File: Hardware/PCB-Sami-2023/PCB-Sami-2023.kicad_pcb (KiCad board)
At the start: 2 copper layers, 75 x 40.2 mm, 44 parts, among them J10 Bateria, J9 STEP_DOWN, P1 TatamiDerecho, P2 TatamiIzquierdo, P3 SharpDerecho, P4 SharpIzquierdo, P5 LDR, P6 MotorIzquierdo, P7 MotorDerecho, P8 Pantalla Oled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

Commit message: agregue ultimos detalles
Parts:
- removed the ? at (113.1, 61.6)
- removed the ? at (113.1, 76.6)
- removed the ? at (113.1, 82.9)
- removed the ? at (135.0, 87.8)
- removed the ? at (113.1, 55.3)
- removed the ? at (146.0, 87.8)
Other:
- board size 75 x 40.2 mm -> 75 x 40 mm
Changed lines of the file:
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@@
     (pad_to_mask_clearance 0)
     (pcbplotparams
-      (layerselection 0x0000010_7ffffffe)
+      (layerselection 0x0000020_7ffffffe)
       (plot_on_all_layers_selection 0x0001000_00000000)
       (disableapertmacros false)
@@
         (effects (font (size 1.27 1.27) (thickness 0.15)))
     )
-    (pad "1" thru_hole circle (at 0 0 180) (size 2 2) (drill 1.00076) (layers "*.Cu" "*.Mask" "F.SilkS")
-      (net 2 "+5V") (pinfunction "1") (pintype "passive"))
-  )
-  (footprint "" (layer "F.Cu")
-    (at 113.1 76.6)
-    (fp_text reference "" (at 0 0) (layer "F.SilkS")
-        (effects (font (size 1.27 1.27) (thickness 0.15)))
-    )
-    (fp_text value "" (at 0 0) (layer "F.SilkS")
-        (effects (font (size 1.27 1.27) (thickness 0.15)))
-    )
     (pad "2" thru_hole circle (at 0 0 180) (size 2 2) (drill 1.00076) (layers "*.Cu" "*.Mask" "F.SilkS")
       (net 6 "/START") (pinfunction "2") (pintype "passive"))
   )
-  (footprint "" (layer "F.Cu")
-    (at 135 87.8)
-    (fp_text reference "" (at 0 0) (layer "F.SilkS")
-        (effects (font (size 1.27 1.27) (thickness 0.15)))
-    )
-    (fp_text value "" (at 0 0) (layer "F.SilkS")
-        (effects (font (size 1.27 1.27) (thickness 0.15)))
-    )
-    (pad "1" thru_hole circle (at 0 0 180) (size 2 2) (drill 1.00076) (layers "*.Cu" "*.Mask" "F.SilkS")
-      (net 2 "+5V") (pinfunction "1") (pintype "passive"))
-  )
-  (footprint "" (layer "F.Cu")
-    (at 113.1 55.3)
-    (fp_text reference "" (at 0 0) (layer "F.SilkS")
-        (effects (font (size 1.27 1.27) (thickness 0.15)))
-    )
-    (fp_text value "" (at 0 0) (layer "F.SilkS")
-        (effects (font (size 1.27 1.27) (thickness 0.15)))
-    )
-    (pad "1" thru_hole circle (at 0 0 180) (size 2 2) (drill 1.00076) (layers "*.Cu" "*.Mask" "F.SilkS")
-      (net 2 "+5V") (pinfunction "1") (pintype "passive"))
-  )
-  (footprint "" (layer "F.Cu")
-    (at 146 87.8)
-    (fp_text reference "" (at 0 0) (layer "F.SilkS")
-        (effects (font (size 1.27 1.27) (thickness 0.15)))
-    )
-    (fp_text value "" (at 0 0) (layer "F.SilkS")
-        (effects (font (size 1.27 1.27) (thickness 0.15)))
-    )
-    (pad "1" thru_hole circle (at 0 0 180) (size 2 2) (drill 1.00076) (layers "*.Cu" "*.Mask" "F.SilkS")
-      (net 2 "+5V") (pinfunction "1") (pintype "passive"))
-  )
   (footprint "EESTN5:Pin_Header_2" (layer "F.Cu")
     (at 177.93 57.2525 180)
@@
       (stroke (width 0) (type solid)) (fill solid) (layer "B.Cu"))
   )
-  (footprint "" (layer "F.Cu")
-    (at 113.1 61.6)
-    (fp_text reference "" (at 0 0) (layer "F.SilkS")
-        (effects (font (size 1.27 1.27) (thickness 0.15)))
-    )
-    (fp_text value "" (at 0 0) (layer "F.SilkS")
-        (effects (font (size 1.27 1.27) (thickness 0.15)))
-    )
-    (pad "1" thru_hole circle (at 0 0 180) (size 2 2) (drill 1.00076) (layers "*.Cu" "*.Mask" "F.SilkS")
-      (net 2 "+5V") (pinfunction "1") (pintype "passive"))
-  )
   (footprint "EESTN5:Pin_Header_2" (layer "F.Cu")
     (at 177.93 61.6175 180)
@@
       (net 6 "/START") (pinfunction "2") (pintype "passive"))
   )
-  (footprint "" (layer "F.Cu")
-    (at 113.1 82.9)
-    (fp_text reference "" (at 0 0) (layer "F.SilkS")
-        (effects (font (size 1.27 1.27) (thickness 0.15)))
-    )
-    (fp_text value "" (at 0 0) (layer "F.SilkS")
-        (effects (font (size 1.27 1.27) (thickness 0.15)))
-    )
-    (pad "1" thru_hole circle (at 0 0 180) (size 2 2) (drill 1.00076) (layers "*.Cu" "*.Mask" "F.SilkS")
-      (net 2 "+5V") (pinfunction "1") (pintype "passive"))
-  )
   (footprint "footprints:JstXH4P" (layer "F.Cu")
     (at 158.3 87.275)
@@
         (effects (font (size 1 1) (thickness 0.15)))
     )
-    (fp_text value "SharpDerecho" (at 0 -1.9) (layer "F.SilkS")
+    (fp_text value "SharpDerecho" (at 10.5 -1.93) (layer "F.SilkS")
         (effects (font (size 1 1) (thickness 0.15)))
     )
@@
   (gr_line (start 106.9 51.65) (end 106.9 91.65)
     (stroke (width 0.1) (type default)) (layer "Edge.Cuts"))
-  (gr_line (start 181.9 91.65) (end 181.9 51.5)
+  (gr_line (start 181.9 91.65) (end 181.9 51.7)
     (stroke (width 0.1) (type default)) (layer "Edge.Cuts"))
   (gr_line (start 181.9 51.65) (end 106.9 51.65)

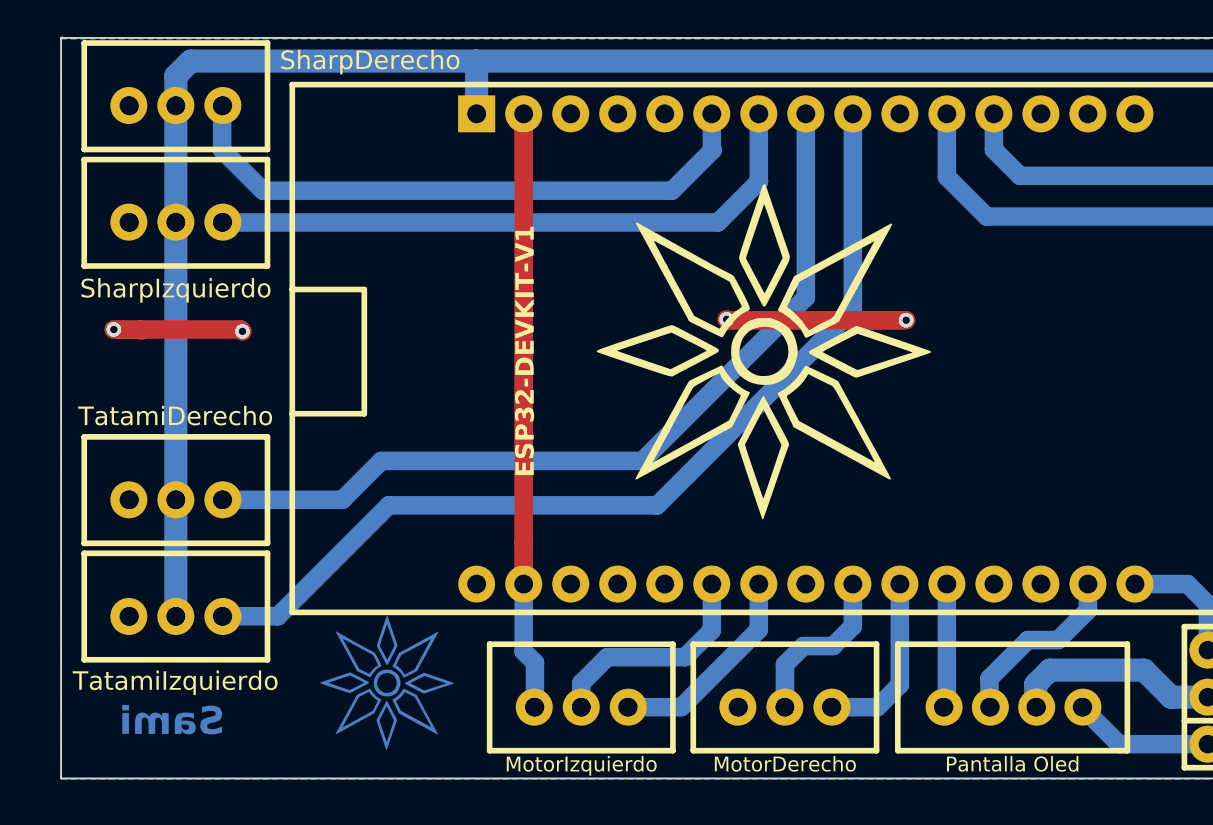
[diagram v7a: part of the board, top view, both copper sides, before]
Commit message: Cambio en el pinout de los motores y unas correcciones de codigos luego de probar el robots
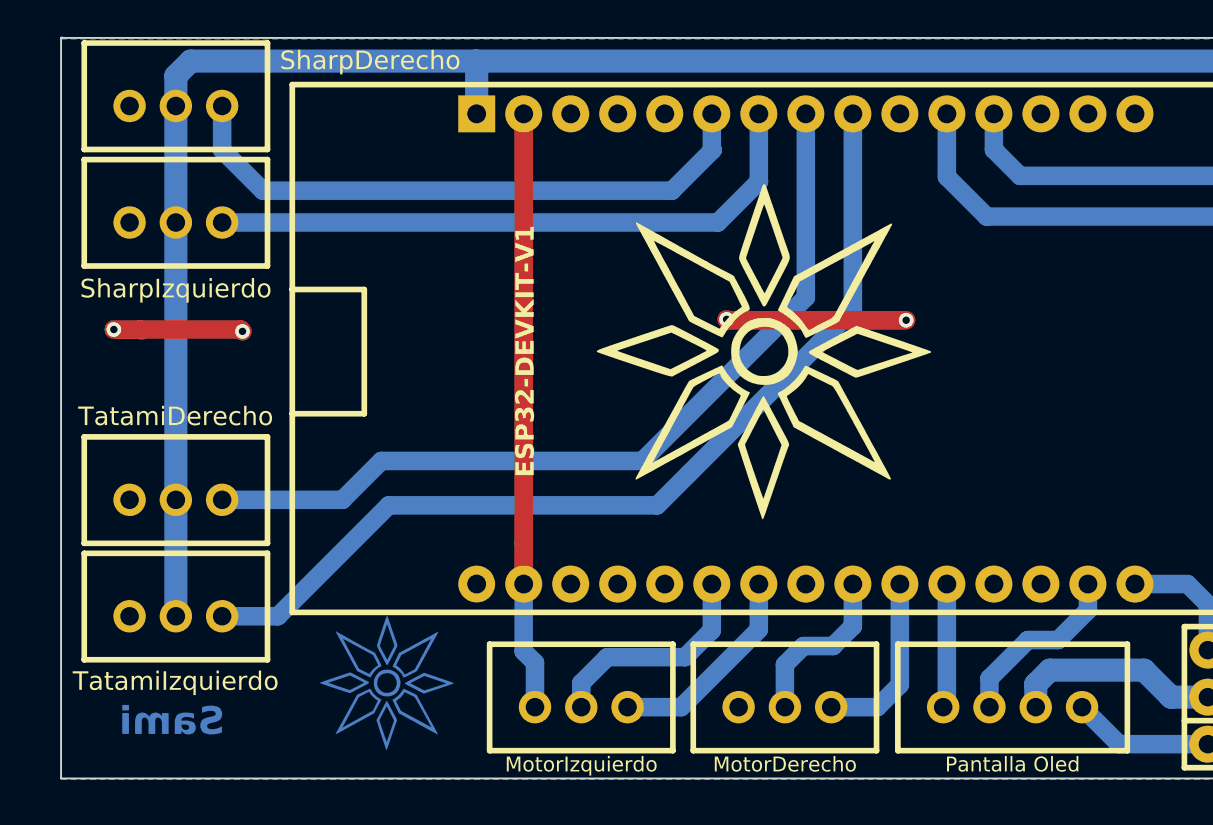
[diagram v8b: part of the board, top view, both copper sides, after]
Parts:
- removed ? (x22): , 
